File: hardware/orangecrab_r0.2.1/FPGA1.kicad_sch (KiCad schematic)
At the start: 14 parts, among them J6 Conn_01x05_Male, U3 LFE5UM-25F-8MG285C, U6 W25Q128JVP

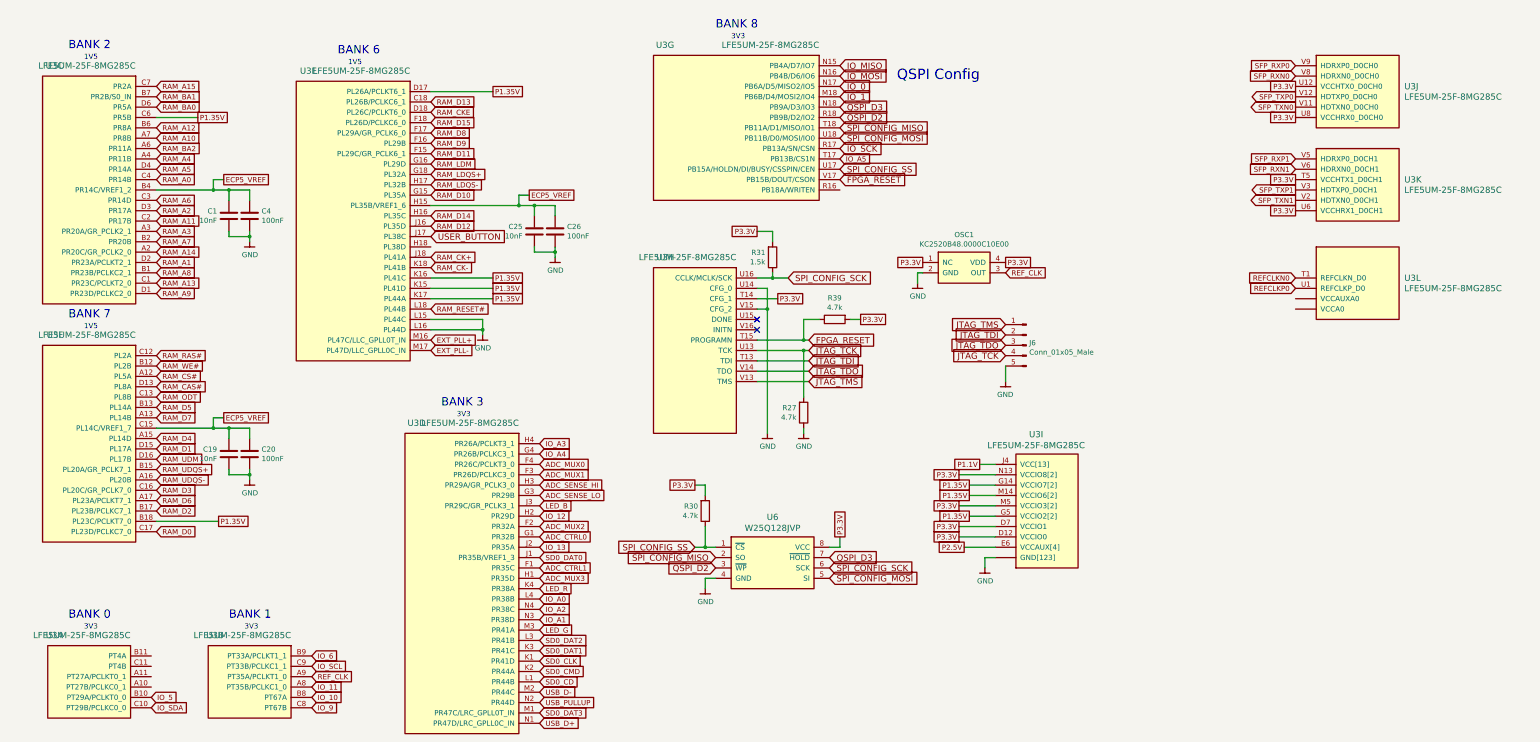
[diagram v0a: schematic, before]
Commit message: Replaced from ECP5U-25 to ECP5UM-25 pinout and added SerDes banks
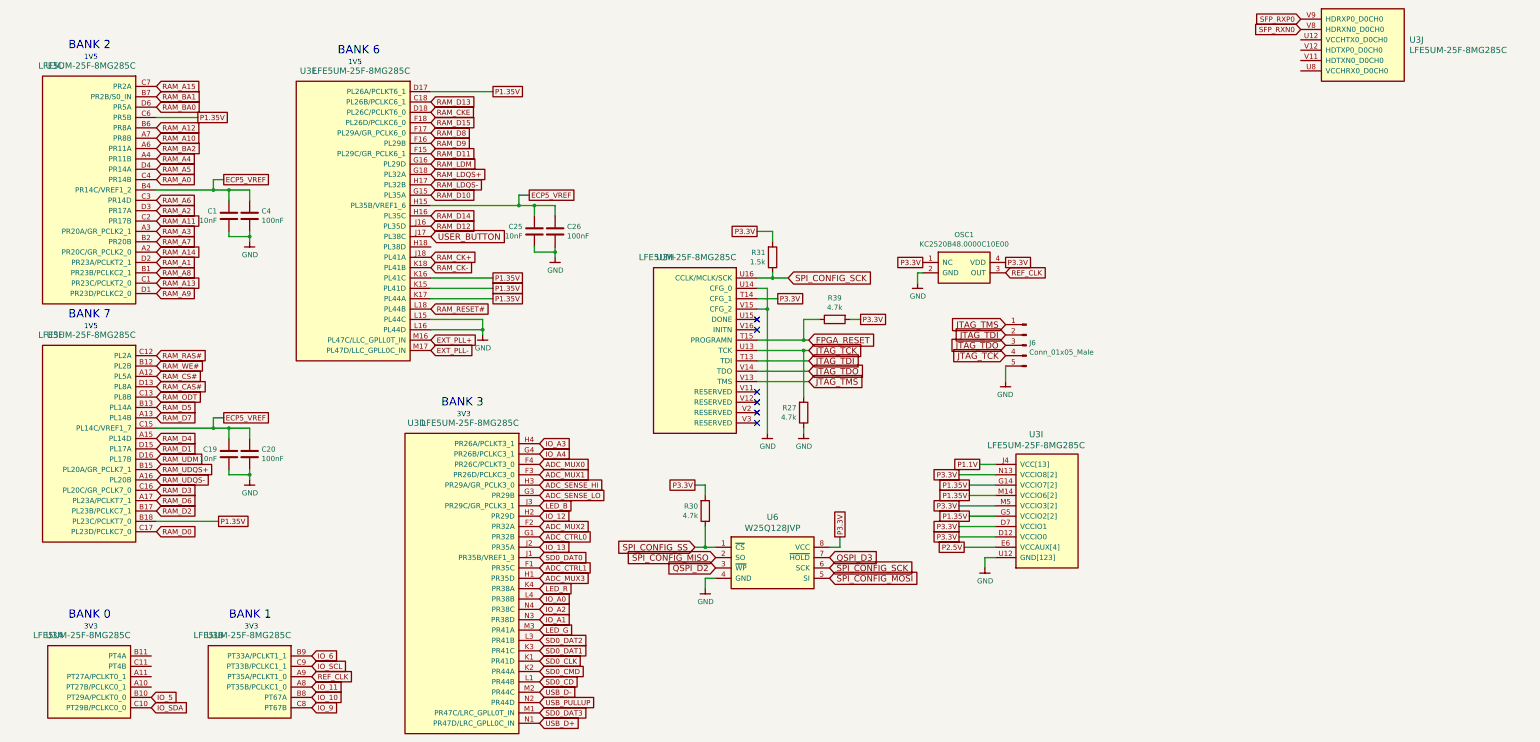
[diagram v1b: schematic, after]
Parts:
- removed unit 12 of U3
- removed unit 11 of U3
- removed unit 7 of U3
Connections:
- net GND: now also U3.P10 (GND[123]), U3.P5 (GND[123]), U3.R10 (GND[123]), U3.R3 (GND[123]), U3.T1 (GND[123]), U3.T5 (GND[123]), U3.U1 (GND[123]), U3.U12 (GND[123]), U3.U6 (GND[123]), U3.U8 (GND[123]), U3.V5 (GND[123]), U3.V6 (GND[123]), U3.V8 (GND[123]), U3.V9 (GND[123])
- net P3.3V: no longer U3.U12 (VCCHTX0_D0CH0), U3.U8 (VCCHRX0_D0CH0)
- net SFP_TXN0: no longer names the net of U3.V11 (HDTXN0_D0CH0)
- net SFP_TXP0: no longer names the net of U3.V12 (HDTXP0_D0CH0)
- no-connect marks 2 -> 6
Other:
- note removed: "BANK 8"
- note removed: "QSPI Config"
- moved on the sheet: U3J
